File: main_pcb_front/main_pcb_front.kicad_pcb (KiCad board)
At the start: 2 copper layers, 95.6 x 95.6 mm, 13 parts

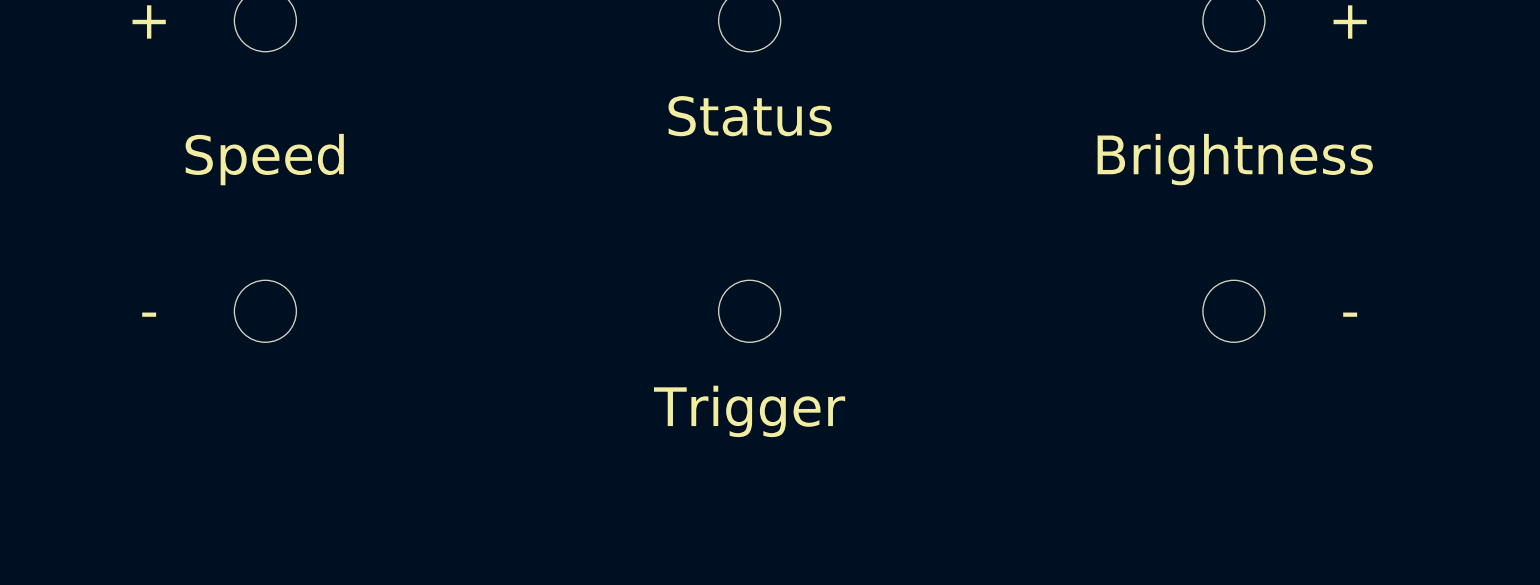
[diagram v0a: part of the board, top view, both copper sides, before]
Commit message: Slightly modification of the front pcb
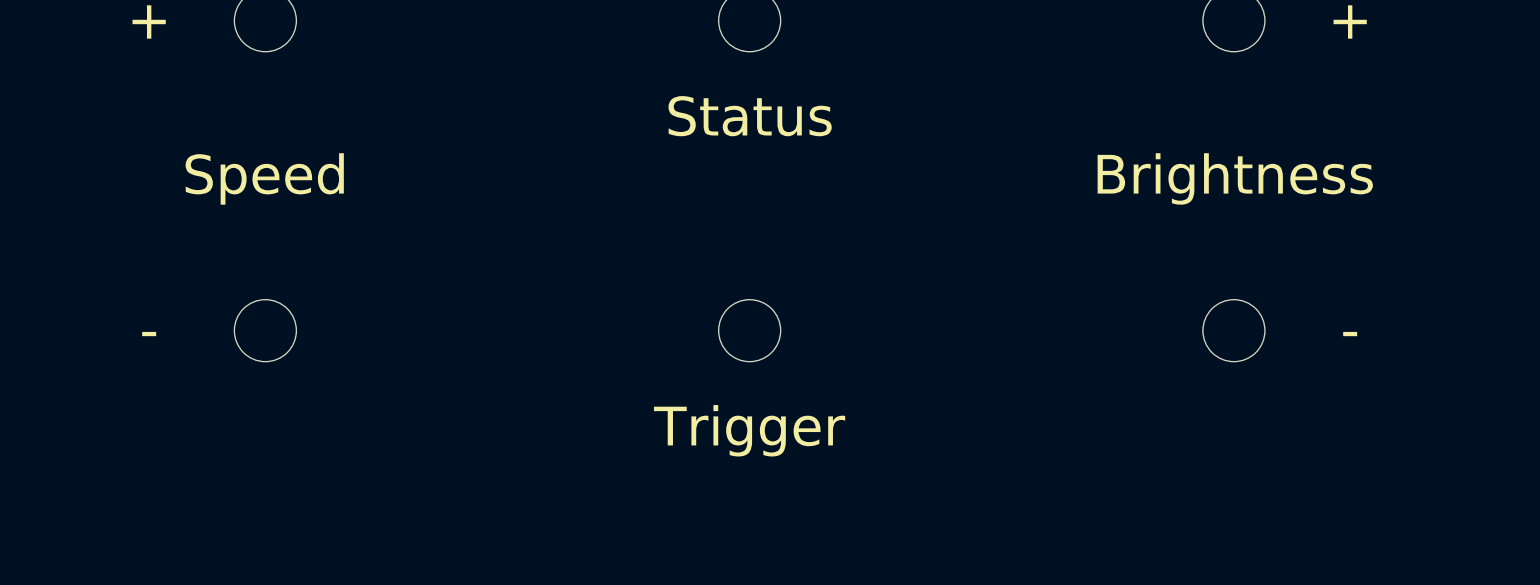
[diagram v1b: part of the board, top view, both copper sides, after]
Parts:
- moved H10 1.00 mm to (173.0, 129.0)
- moved H6 1.00 mm to (123.0, 129.0)
- moved H8 1.00 mm to (148.0, 129.0)

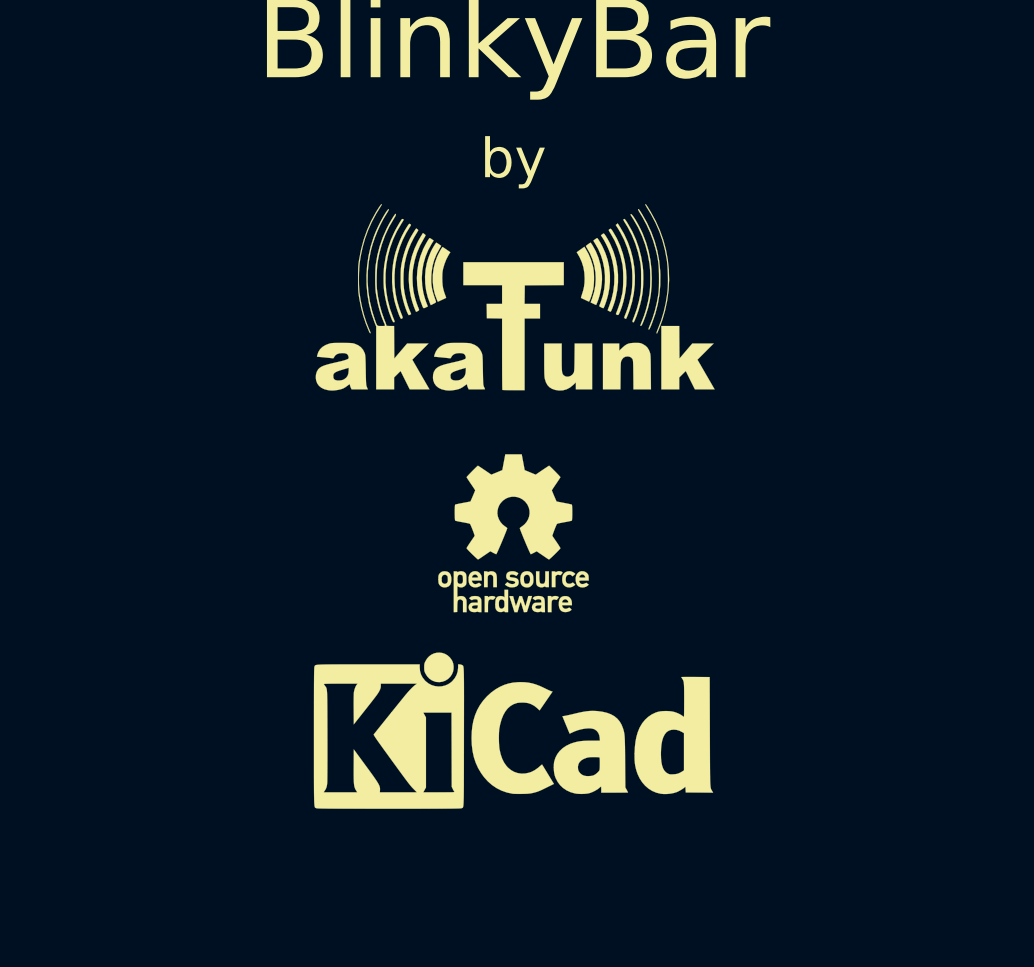
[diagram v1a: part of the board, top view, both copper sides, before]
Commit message: Updated layout
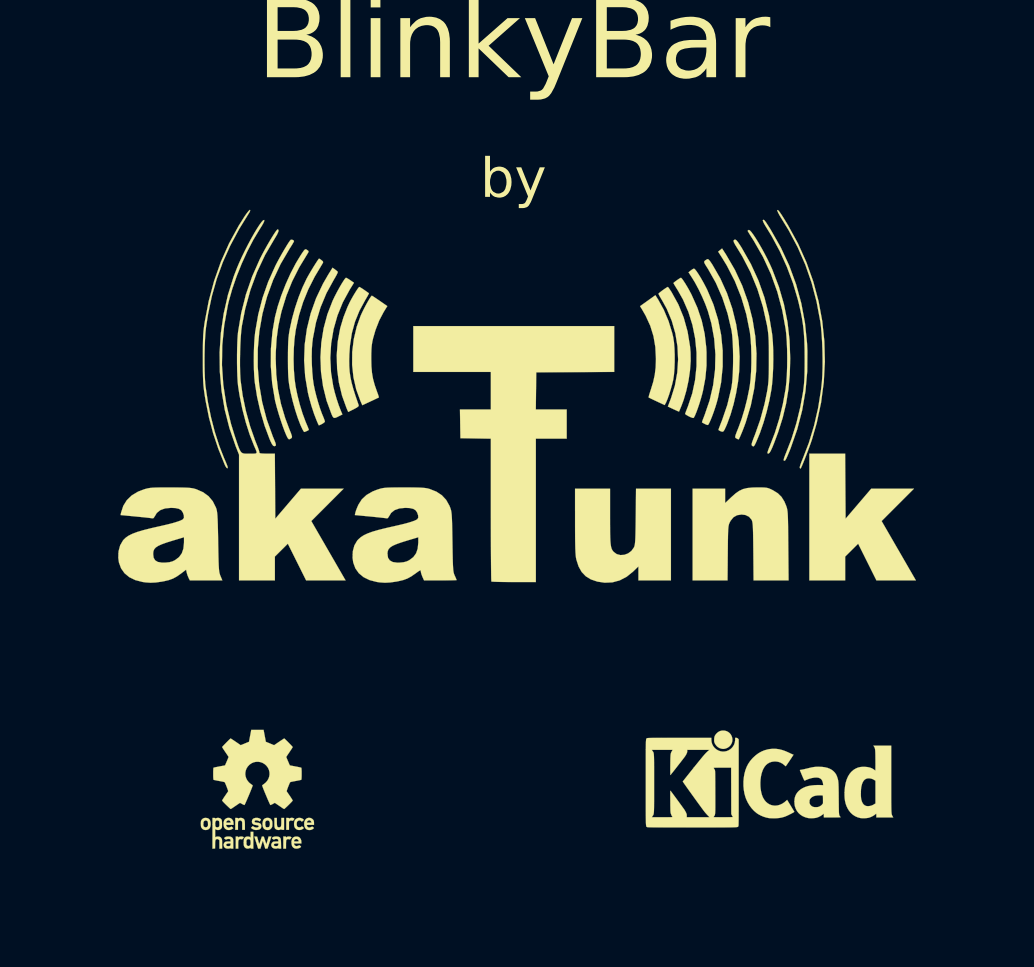
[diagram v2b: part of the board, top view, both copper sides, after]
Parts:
- removed the REF** at (148.0, 95.0)
- removed the REF** at (148.0, 85.0)
- added REF**: OSHW-Logo_5.7x6mm_SilkScreen, Symbol:OSHW-Logo_5.7x6mm_SilkScreen, F.Cu at (135.0, 98.0)
- added REF**: KiCad-Logo_5mm_SilkScreen, Symbol:KiCad-Logo_5mm_SilkScreen, F.Cu at (161.0, 98.0)
- moved G*** 5.00 mm to (148.0, 78.0)

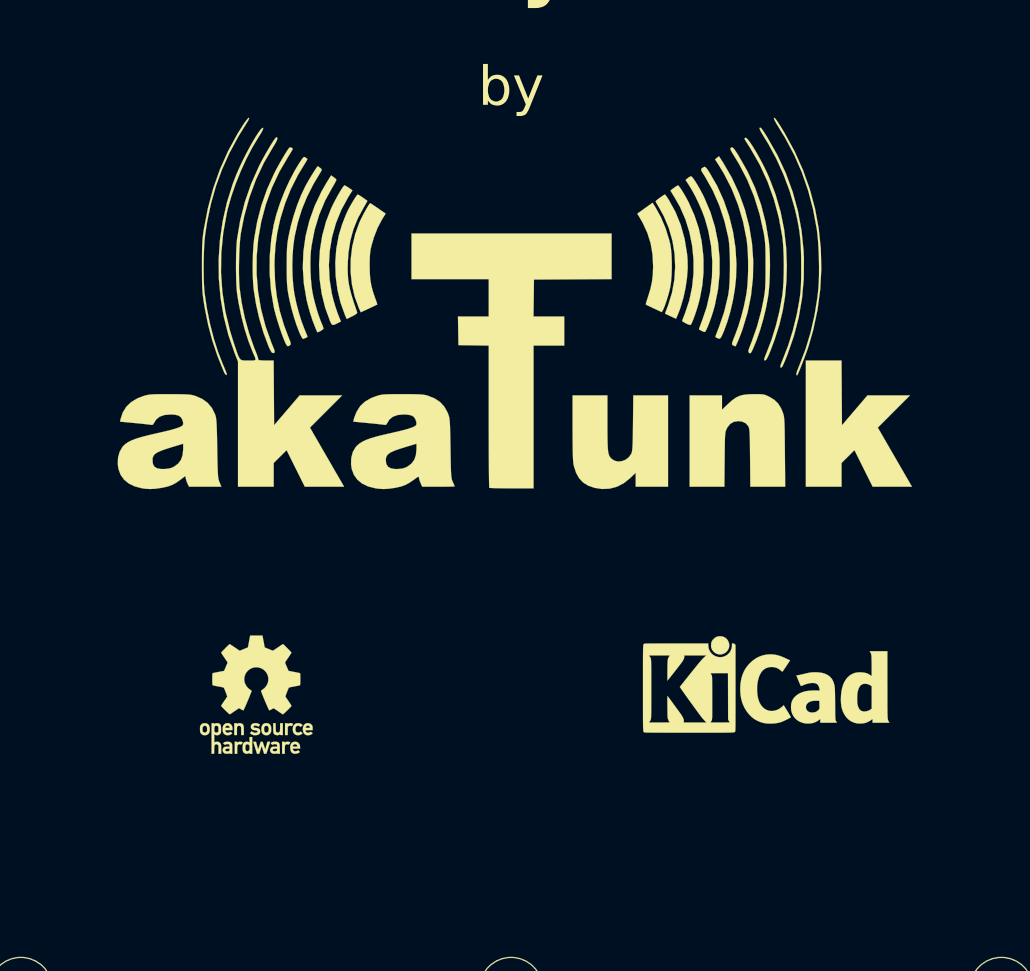
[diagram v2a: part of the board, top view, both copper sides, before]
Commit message: Added power button and its protector to the front pcb
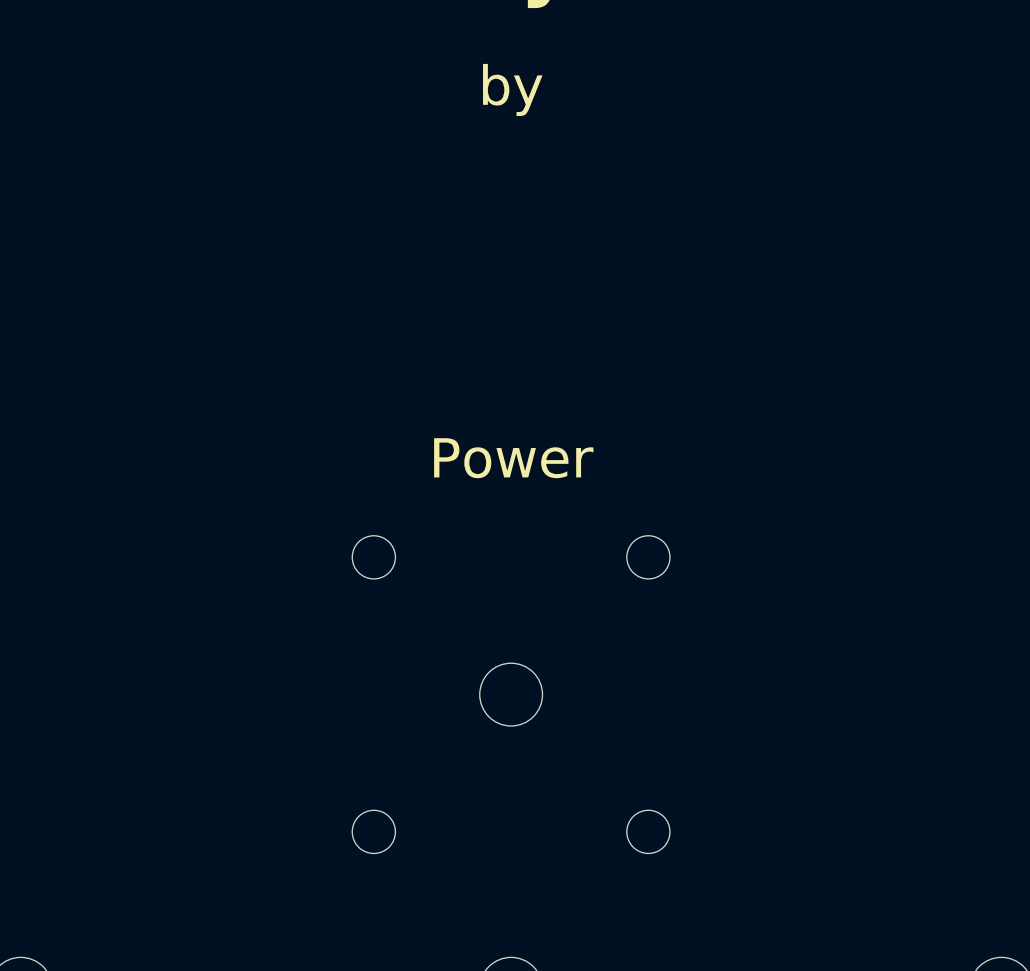
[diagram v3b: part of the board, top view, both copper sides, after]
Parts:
- removed G***: LOGO, akaFunkLogo:akaFunkLogo
- removed REF**: OSHW-Logo_5.7x6mm_SilkScreen, Symbol:OSHW-Logo_5.7x6mm_SilkScreen
- removed REF**: KiCad-Logo_5mm_SilkScreen, Symbol:KiCad-Logo_5mm_SilkScreen
- added H11: PWR, main_pcb_front:MountingHole_PowerBtn, F.Cu at (148.0, 98.0)
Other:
- board text added: "Power"

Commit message: Added akaFunk logo to front panel
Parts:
- added G***: LOGO, akaFunkLogo:akaFunkLogo, F.Cu at (148.0, 69.5)
